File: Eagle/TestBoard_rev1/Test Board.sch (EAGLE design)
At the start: 8 parts

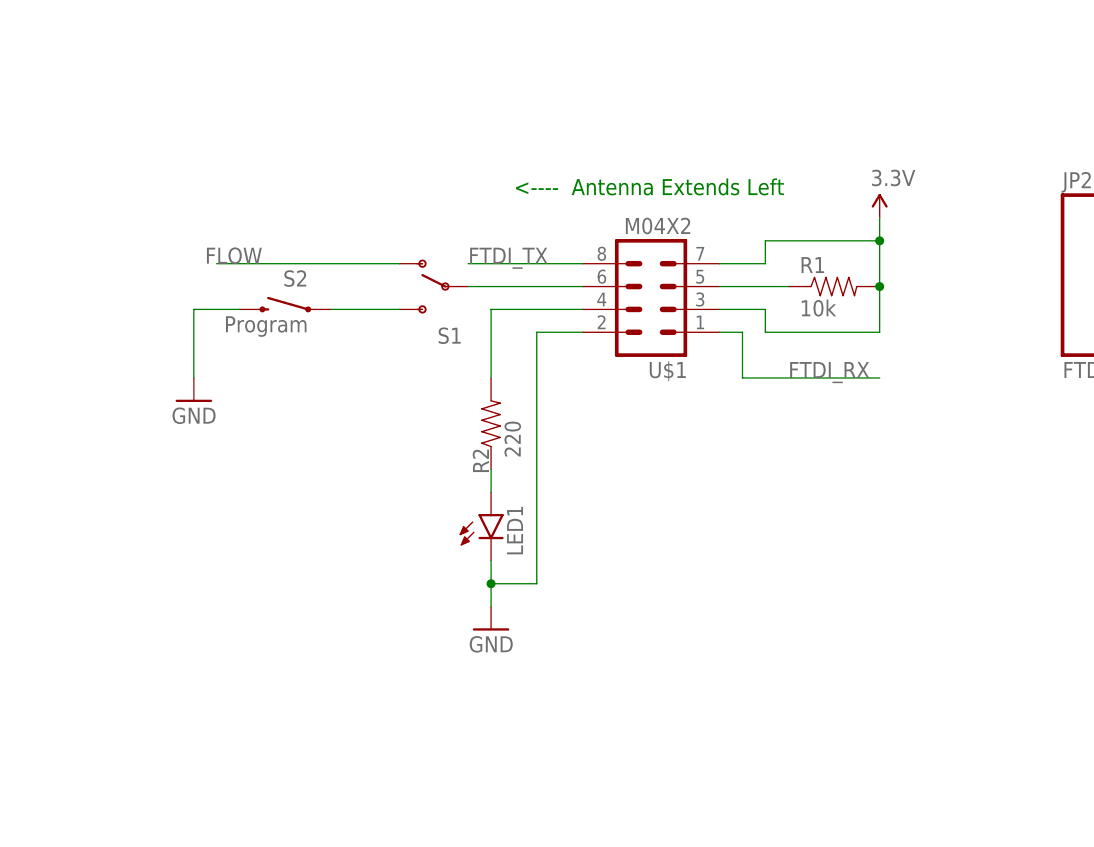
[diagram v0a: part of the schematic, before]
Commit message: I don't like your organization Ward...
Moved the Eagle Schematic to a better spot for organization purposes and
Rearranged the schematic while adding some labels to better suit style
guidelines for readability.
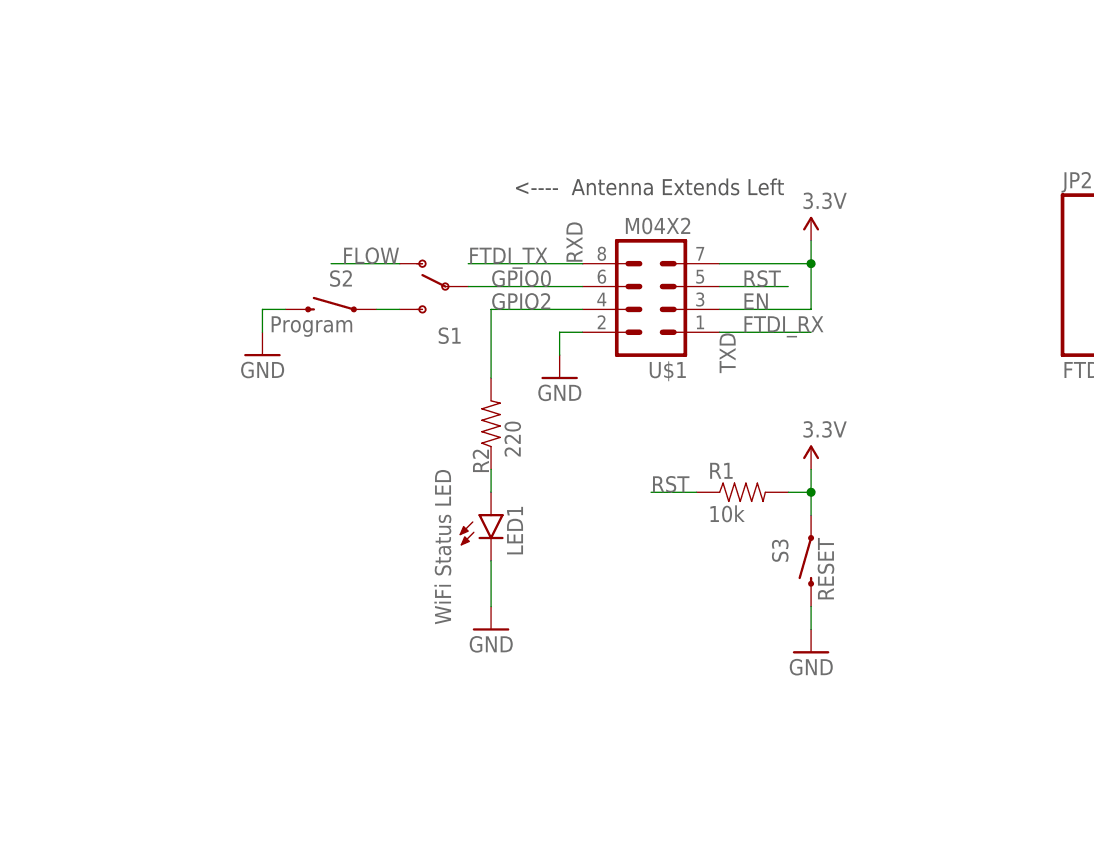
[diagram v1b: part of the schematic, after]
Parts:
- added S3: RESET, SparkFun-Electromechanical:SWITCH-MOMENTARY-2PTH
- LED1: value (none) -> WiFi Status LED
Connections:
- net N$2 renamed RST
- net N$3 renamed GPIO2
- net N$4 renamed GPIO0
- net 3.3V: now also S3.1
- net GND: now also S3.2
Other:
- note added: "EN"
- note added: "RXD"
- note added: "TXD"
- moved on the sheet: R1, S2
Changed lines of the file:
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@@
 <part name="JP2" library="SparkFun-Connectors" deviceset="FTDI_BASIC" device="PTH"/>
 <part name="U$1" library="SparkFun-Connectors" deviceset="M04X2" device=""/>
-<part name="R1" library="SparkFun-Resistors" deviceset="RESISTOR" device="AXIAL-0.3" value="10k"/>
 <part name="SUPPLY1" library="SparkFun-Aesthetics" deviceset="3.3V" device=""/>
 <part name="R2" library="SparkFun-Resistors" deviceset="RESISTOR" device="AXIAL-0.3" value="220"/>
-<part name="LED1" library="SparkFun-LED" deviceset="LED" device="-3MM-NO_SILK"/>
+<part name="LED1" library="SparkFun-LED" deviceset="LED" device="-3MM-NO_SILK" value="WiFi Status LED"/>
 <part name="GND3" library="SparkFun-Aesthetics" deviceset="GND" device=""/>
+<part name="S3" library="SparkFun-Electromechanical" deviceset="SWITCH-MOMENTARY-2" device="PTH" value="RESET"/>
+<part name="R1" library="SparkFun-Resistors" deviceset="RESISTOR" device="AXIAL-0.3" value="10k"/>
+<part name="GND4" library="SparkFun-Aesthetics" deviceset="GND" device=""/>
+<part name="SUPPLY2" library="SparkFun-Aesthetics" deviceset="3.3V" device=""/>
+<part name="GND5" library="SparkFun-Aesthetics" deviceset="GND" device=""/>
 </parts>
 <sheets>
 <sheet>
 <plain>
-<text x="88.9" y="124.46" size="1.778" layer="91">&lt;----  Antenna Extends Left</text>
+<text x="88.9" y="124.46" size="1.778" layer="97">&lt;----  Antenna Extends Left</text>
 <text x="160.274" y="1.524" size="1.778" layer="91">4/28/15</text>
 <text x="232.918" y="1.27" size="1.778" layer="91">1/1</text>
 <text x="241.3" y="7.62" size="1.778" layer="91">1.0</text>
+<text x="114.3" y="111.76" size="1.778" layer="95">EN</text>
+<text x="96.52" y="116.84" size="1.778" layer="95" rot="R90">RXD</text>
+<text x="111.76" y="109.22" size="1.778" layer="95" rot="R270">TXD</text>
 </plain>
 <instances>
@@
 <instance part="FRAME1" gate="G$2" x="147.32" y="0"/>
 <instance part="S1" gate="1" x="81.28" y="114.3" rot="MR0"/>
-<instance part="S2" gate="G$1" x="63.5" y="111.76" rot="MR0"/>
-<instance part="GND1" gate="1" x="53.34" y="101.6" rot="MR0"/>
+<instance part="S2" gate="G$1" x="68.58" y="111.76" rot="MR0"/>
+<instance part="GND1" gate="1" x="60.96" y="106.68" rot="MR0"/>
 <instance part="GND2" gate="1" x="180.34" y="116.84"/>
 <instance part="JP2" gate="G$1" x="154.94" y="114.3"/>
 <instance part="U$1" gate="G$1" x="104.14" y="114.3" rot="R180"/>
-<instance part="R1" gate="G$1" x="124.46" y="114.3"/>
-<instance part="SUPPLY1" gate="G$1" x="129.54" y="121.92"/>
+<instance part="SUPPLY1" gate="G$1" x="121.92" y="119.38"/>
 <instance part="R2" gate="G$1" x="86.36" y="99.06" smashed="yes" rot="R90">
 <attribute name="NAME" x="86.1314" y="93.472" size="1.778" layer="95" rot="R90"/>
 <attribute name="VALUE" x="89.662" y="95.25" size="1.778" layer="96" rot="R90"/>
 </instance>
-<instance part="LED1" gate="G$1" x="86.36" y="88.9"/>
+<instance part="LED1" gate="G$1" x="86.36" y="88.9" smashed="yes">
+<attribute name="NAME" x="89.916" y="84.328" size="1.778" layer="95" rot="R90"/>
+<attribute name="VALUE" x="81.915" y="76.708" size="1.778" layer="96" rot="R90"/>
+</instance>
 <instance part="GND3" gate="1" x="86.36" y="76.2" rot="MR0"/>
+<instance part="S3" gate="G$1" x="121.92" y="83.82" rot="MR270"/>
+<instance part="R1" gate="G$1" x="114.3" y="91.44"/>
+<instance part="GND4" gate="1" x="93.98" y="104.14" rot="MR0"/>
+<instance part="SUPPLY2" gate="G$1" x="121.92" y="93.98"/>
+<instance part="GND5" gate="1" x="121.92" y="73.66" rot="MR0"/>
 </instances>
 <busses>
@@
 <segment>
 <pinref part="S1" gate="1" pin="O"/>
-<wire x1="76.2" y1="116.84" x2="55.88" y2="116.84" width="0.1524" layer="91"/>
-<label x="60.96" y="116.84" size="1.778" layer="95" rot="MR0"/>
+<wire x1="76.2" y1="116.84" x2="68.58" y2="116.84" width="0.1524" layer="91"/>
+<label x="76.2" y="116.84" size="1.778" layer="95" rot="MR0"/>
 </segment>
 </net>
@@
 <pinref part="S1" gate="1" pin="S"/>
 <pinref part="S2" gate="G$1" pin="1"/>
-<wire x1="76.2" y1="111.76" x2="68.58" y2="111.76" width="0.1524" layer="91"/>
+<wire x1="76.2" y1="111.76" x2="73.66" y2="111.76" width="0.1524" layer="91"/>
 </segment>
 </net>
@@
 <segment>
 <pinref part="S2" gate="G$1" pin="2"/>
-<wire x1="58.42" y1="111.76" x2="53.34" y2="111.76" width="0.1524" layer="91"/>
-<wire x1="53.34" y1="111.76" x2="53.34" y2="104.14" width="0.1524" layer="91"/>
+<wire x1="63.5" y1="111.76" x2="60.96" y2="111.76" width="0.1524" layer="91"/>
+<wire x1="60.96" y1="111.76" x2="60.96" y2="109.22" width="0.1524" layer="91"/>
 <pinref part="GND1" gate="1" pin="GND"/>
 </segment>
@@
 </segment>
 <segment>
+<pinref part="GND3" gate="1" pin="GND"/>
 <pinref part="LED1" gate="G$1" pin="C"/>
-<pinref part="GND3" gate="1" pin="GND"/>
-<wire x1="86.36" y1="83.82" x2="86.36" y2="81.28" width="0.1524" layer="91"/>
+<wire x1="86.36" y1="83.82" x2="86.36" y2="78.74" width="0.1524" layer="91"/>
+</segment>
+<segment>
 <pinref part="U$1" gate="G$1" pin="2"/>
-<wire x1="86.36" y1="81.28" x2="86.36" y2="78.74" width="0.1524" layer="91"/>
-<wire x1="96.52" y1="109.22" x2="91.44" y2="109.22" width="0.1524" layer="91"/>
-<wire x1="91.44" y1="109.22" x2="91.44" y2="81.28" width="0.1524" layer="91"/>
-<wire x1="91.44" y1="81.28" x2="86.36" y2="81.28" width="0.1524" layer="91"/>
-<junction x="86.36" y="81.28"/>
+<wire x1="96.52" y1="109.22" x2="93.98" y2="109.22" width="0.1524" layer="91"/>
+<pinref part="GND4" gate="1" pin="GND"/>
+<wire x1="93.98" y1="106.68" x2="93.98" y2="109.22" width="0.1524" layer="91"/>
+</segment>
+<segment>
+<pinref part="S3" gate="G$1" pin="2"/>
+<pinref part="GND5" gate="1" pin="GND"/>
+<wire x1="121.92" y1="78.74" x2="121.92" y2="76.2" width="0.1524" layer="91"/>
 </segment>
 </net>
@@
 <segment>
 <pinref part="U$1" gate="G$1" pin="1"/>
-<wire x1="111.76" y1="109.22" x2="114.3" y2="109.22" width="0.1524" layer="91"/>
-<wire x1="114.3" y1="109.22" x2="114.3" y2="104.14" width="0.1524" layer="91"/>
-<wire x1="114.3" y1="104.14" x2="129.54" y2="104.14" width="0.1524" layer="91"/>
-<label x="119.38" y="104.14" size="1.778" layer="95"/>
+<wire x1="111.76" y1="109.22" x2="121.92" y2="109.22" width="0.1524" layer="91"/>
+<label x="114.3" y="109.22" size="1.778" layer="95"/>
 </segment>
 </net>
@@
 </segment>
 </net>
-<net name="N$2" class="0">
+<net name="RST" class="0">
 <segment>
 <pinref part="U$1" gate="G$1" pin="5"/>
+<wire x1="111.76" y1="114.3" x2="119.38" y2="114.3" width="0.1524" layer="91"/>
+<label x="114.3" y="114.3" size="1.778" layer="95"/>
+</segment>
+<segment>
 <pinref part="R1" gate="G$1" pin="1"/>
-<wire x1="111.76" y1="114.3" x2="119.38" y2="114.3" width="0.1524" layer="91"/>
+<wire x1="109.22" y1="91.44" x2="104.14" y2="91.44" width="0.1524" layer="91"/>
+<label x="104.14" y="91.44" size="1.778" layer="95"/>
 </segment>
 </net>
 <net name="3.3V" class="0">
 <segment>
+<pinref part="SUPPLY1" gate="G$1" pin="3.3V"/>
+<wire x1="121.92" y1="116.84" x2="121.92" y2="119.38" width="0.1524" layer="91"/>
+<pinref part="U$1" gate="G$1" pin="7"/>
+<wire x1="111.76" y1="116.84" x2="121.92" y2="116.84" width="0.1524" layer="91"/>
+<pinref part="U$1" gate="G$1" pin="3"/>
+<wire x1="111.76" y1="111.76" x2="121.92" y2="111.76" width="0.1524" layer="91"/>
+<wire x1="121.92" y1="111.76" x2="121.92" y2="116.84" width="0.1524" layer="91"/>
+<junction x="121.92" y="116.84"/>
+</segment>
+<segment>
 <pinref part="R1" gate="G$1" pin="2"/>
-<wire x1="129.54" y1="114.3" x2="129.54" y2="119.38" width="0.1524" layer="91"/>
-<pinref part="SUPPLY1" gate="G$1" pin="3.3V"/>
-<pinref part="U$1" gate="G$1" pin="3"/>
-<wire x1="129.54" y1="119.38" x2="129.54" y2="121.92" width="0.1524" layer="91"/>
-<wire x1="111.76" y1="111.76" x2="116.84" y2="111.76" width="0.1524" layer="91"/>
-<wire x1="116.84" y1="111.76" x2="116.84" y2="109.22" width="0.1524" layer="91"/>
-<wire x1="116.84" y1="109.22" x2="129.54" y2="109.22" width="0.1524" layer="91"/>
-<wire x1="129.54" y1="109.22" x2="129.54" y2="114.3" width="0.1524" layer="91"/>
-<junction x="129.54" y="114.3"/>
-<pinref part="U$1" gate="G$1" pin="7"/>
-<wire x1="111.76" y1="116.84" x2="116.84" y2="116.84" width="0.1524" layer="91"/>
-<wire x1="116.84" y1="116.84" x2="116.84" y2="119.38" width="0.1524" layer="91"/>
-<wire x1="116.84" y1="119.38" x2="129.54" y2="119.38" width="0.1524" layer="91"/>
-<junction x="129.54" y="119.38"/>
+<wire x1="119.38" y1="91.44" x2="121.92" y2="91.44" width="0.1524" layer="91"/>
+<pinref part="S3" gate="G$1" pin="1"/>
+<wire x1="121.92" y1="91.44" x2="121.92" y2="88.9" width="0.1524" layer="91"/>
+<pinref part="SUPPLY2" gate="G$1" pin="3.3V"/>
+<wire x1="121.92" y1="93.98" x2="121.92" y2="91.44" width="0.1524" layer="91"/>
+<junction x="121.92" y="91.44"/>
 </segment>
 </net>
-<net name="N$4" class="0">
+<net name="GPIO0" class="0">
 <segment>
 <pinref part="S1" gate="1" pin="P"/>
 <pinref part="U$1" gate="G$1" pin="6"/>
 <wire x1="83.82" y1="114.3" x2="96.52" y2="114.3" width="0.1524" layer="91"/>
+<label x="86.36" y="114.3" size="1.778" layer="95"/>
 </segment>
 </net>
-<net name="N$3" class="0">
+<net name="GPIO2" class="0">
 <segment>
 <pinref part="U$1" gate="G$1" pin="4"/>
@@
 <wire x1="96.52" y1="111.76" x2="86.36" y2="111.76" width="0.1524" layer="91"/>
 <wire x1="86.36" y1="111.76" x2="86.36" y2="104.14" width="0.1524" layer="91"/>
+<label x="86.36" y="111.76" size="1.778" layer="95"/>
 </segment>
 </net>
